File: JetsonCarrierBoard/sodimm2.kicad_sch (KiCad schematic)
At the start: 1 part

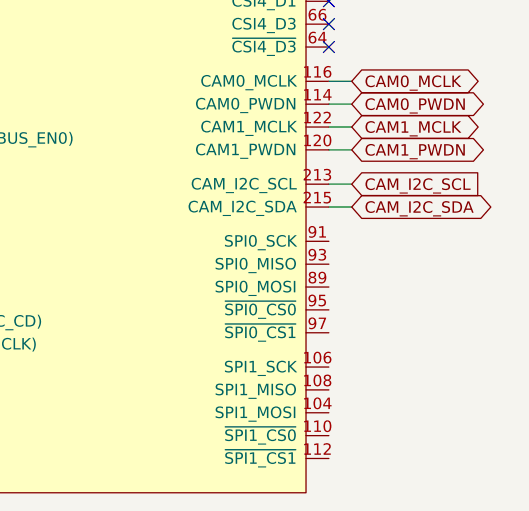
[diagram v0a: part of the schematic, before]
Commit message: IMU wiring
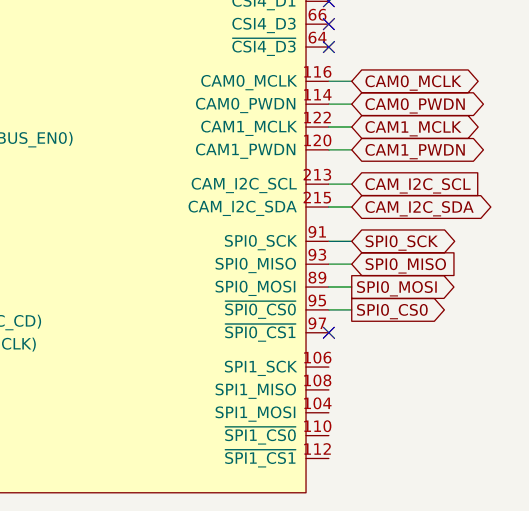
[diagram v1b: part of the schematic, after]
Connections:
- net SPI0_MOSI: now reaches J?.89 (SPI0_MOSI)
- net SPI0_SCK: now reaches J?.91 (SPI0_SCK)
- net SPI0_MISO: now reaches J?.93 (SPI0_MISO)
- net SPI0_CS0: now reaches J?.95 (~{SPI0_CS0})
- no-connect marks 39 -> 40
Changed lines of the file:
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@@
   (no_connect (at 170.18 54.61))
   (no_connect (at 170.18 57.15))
+  (no_connect (at 170.18 148.59))
   (no_connect (at 170.18 90.17))
   (no_connect (at 170.18 93.98))
@@
     (stroke (width 0) (type default) (color 0 0 0 0))
   )
+  (wire (pts (xy 170.18 138.43) (xy 172.72 138.43))
+    (stroke (width 0) (type default) (color 0 0 0 0))
+  )
   (wire (pts (xy 170.18 120.65) (xy 172.72 120.65))
     (stroke (width 0) (type default) (color 0 0 0 0))
@@
     (stroke (width 0) (type default) (color 0 0 0 0))
   )
+  (wire (pts (xy 170.18 146.05) (xy 172.72 146.05))
+    (stroke (width 0) (type default) (color 0 0 0 0))
+  )
   (wire (pts (xy 170.18 134.62) (xy 172.72 134.62))
     (stroke (width 0) (type default) (color 0 0 0 0))
@@
     (stroke (width 0) (type default) (color 0 0 0 0))
   )
+  (wire (pts (xy 170.18 143.51) (xy 172.72 143.51))
+    (stroke (width 0) (type default) (color 0 0 0 0))
+  )
   (wire (pts (xy 170.18 38.1) (xy 172.72 38.1))
     (stroke (width 0) (type default) (color 0 0 0 0))
@@
     (stroke (width 0) (type default) (color 0 0 0 0))
   )
+  (wire (pts (xy 170.18 140.97) (xy 172.72 140.97))
+    (stroke (width 0) (type default) (color 0 0 0 0))
+  )
   (wire (pts (xy 107.95 54.61) (xy 116.84 54.61))
     (stroke (width 0) (type default) (color 0 0 0 0))
@@
     )
   )
+  (global_label "SPI0_SCK" (shape bidirectional) (at 172.72 138.43 0) (fields_autoplaced)
+    (effects (font (size 1.27 1.27)) (justify left))
+    (property "Intersheet References" "${INTERSHEET_REFS}" (id 0) (at 184.1441 138.3506 0)
+      (effects (font (size 1.27 1.27)) (justify left) hide)
+    )
+  )
   (global_label "CAM0_PWDN" (shape bidirectional) (at 172.72 123.19 0) (fields_autoplaced)
     (effects (font (size 1.27 1.27)) (justify left))
@@
     )
   )
+  (global_label "SPI0_CS0" (shape output) (at 172.72 146.05 0) (fields_autoplaced)
+    (effects (font (size 1.27 1.27)) (justify left))
+    (property "Intersheet References" "${INTERSHEET_REFS}" (id 0) (at 184.0836 145.9706 0)
+      (effects (font (size 1.27 1.27)) (justify left) hide)
+    )
+  )
   (global_label "I2S1_SCLK" (shape bidirectional) (at 107.95 66.04 180) (fields_autoplaced)
     (effects (font (size 1.27 1.27)) (justify right))
@@
     )
   )
+  (global_label "SPI0_MISO" (shape input) (at 172.72 140.97 0) (fields_autoplaced)
+    (effects (font (size 1.27 1.27)) (justify left))
+    (property "Intersheet References" "${INTERSHEET_REFS}" (id 0) (at 184.9907 140.8906 0)
+      (effects (font (size 1.27 1.27)) (justify left) hide)
+    )
+  )
   (global_label "MIC_SCK" (shape bidirectional) (at 107.95 54.61 180) (fields_autoplaced)
     (effects (font (size 1.27 1.27)) (justify right))
@@
       (effects (font (size 1.27 1.27)) (justify left) hide)
     )
+  )
+  (global_label "SPI0_MOSI" (shape output) (at 172.72 143.51 0) (fields_autoplaced)
+    (effects (font (size 1.27 1.27)) (justify left))
+    (property "Intersheet References" "${INTERSHEET_REFS}" (id 0) (at 184.9907 143.4306 0)
+      (effects (font (size 1.27 1.27)) (justify left) hide)
+    )

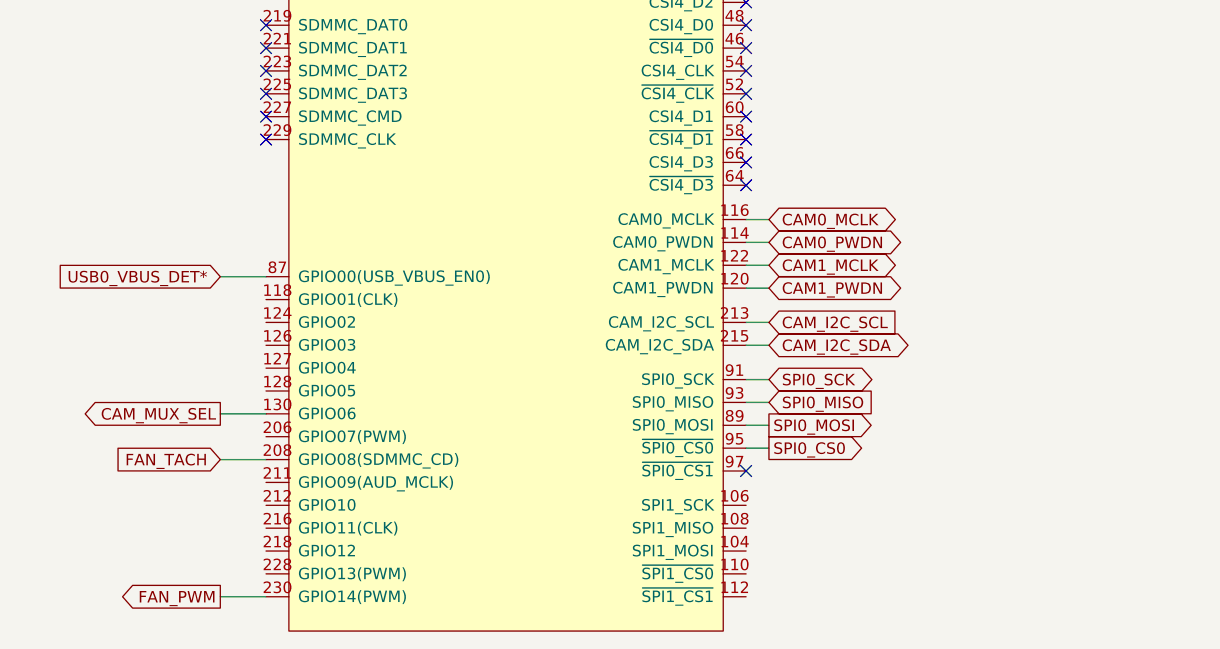
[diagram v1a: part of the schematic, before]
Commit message: Added basic circuits, LED circuit, GPIO pins in GPIO page
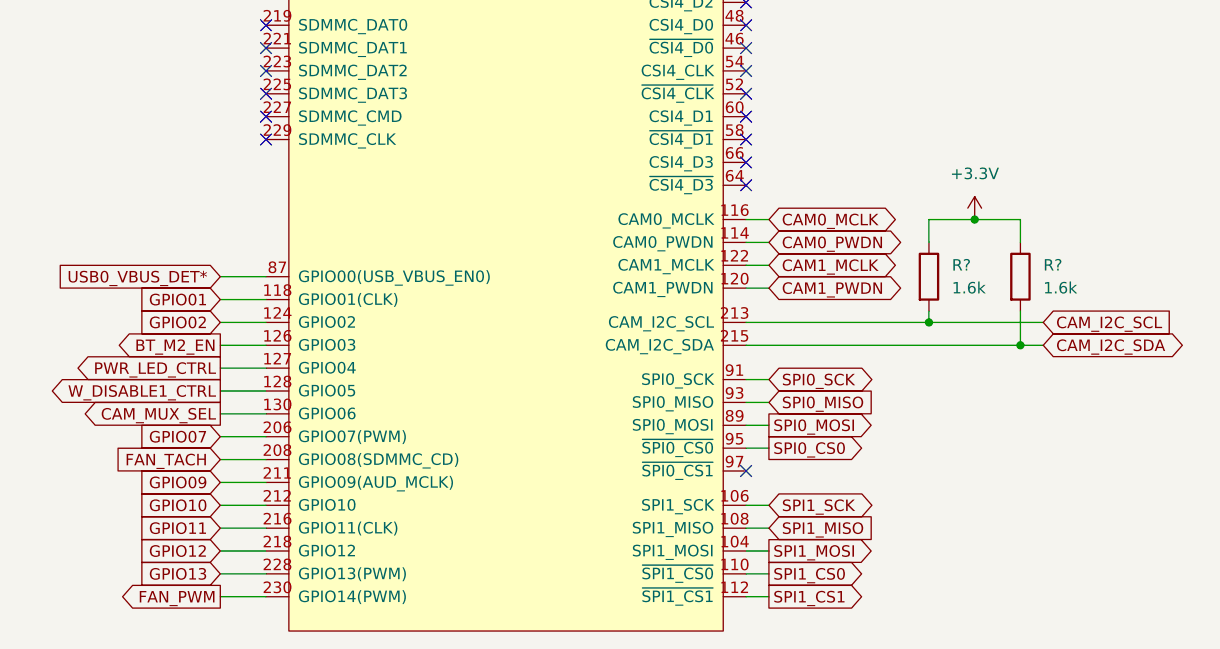
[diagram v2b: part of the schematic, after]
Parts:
- added R? (x2): 1.6k, symbol Device:R
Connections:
- net CAM_I2C_SCL: now also R?.2
- net CAM_I2C_SDA: now also R?.2
- net SPI1_MOSI: now reaches J?.104 (SPI1_MOSI)
- net SPI1_SCK: now reaches J?.106 (SPI1_SCK)
- net SPI1_MISO: now reaches J?.108 (SPI1_MISO)
- net SPI1_CS0: now reaches J?.110 (~{SPI1_CS0})
- net SPI1_CS1: now reaches J?.112 (~{SPI1_CS1})
- net GPIO01: now reaches J?.118 (GPIO01(CLK))
- net GPIO02: now reaches J?.124 (GPIO02)
- net BT_M2_EN: now reaches J?.126 (GPIO03)
- net PWR_LED_CTRL: now reaches J?.127 (GPIO04)
- net W_DISABLE1_CTRL: now reaches J?.128 (GPIO05)
- net GPIO07: now reaches J?.206 (GPIO07(PWM))
- net GPIO09: now reaches J?.211 (GPIO09(AUD_MCLK))
- net GPIO10: now reaches J?.212 (GPIO10)
- net GPIO11: now reaches J?.216 (GPIO11(CLK))
- net GPIO12: now reaches J?.218 (GPIO12)
- net GPIO13: now reaches J?.228 (GPIO13(PWM))
- new net +3.3V: R?.1, R?.1

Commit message: Adding more Title block info and changing main hierarchical page layout
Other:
- title: (none) -> SODIMM Connector 2/3
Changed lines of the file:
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@@
 (kicad_sch (version 20211123) (generator eeschema)
   (paper "A4")
+  (title_block
+    (title "SODIMM Connector 2/3")
+    (date "2022-09-18")
+    (rev "1.0")
+  )
   (junction (at 190.5 132.08) (diameter 0) (color 0 0 0 0)
   )

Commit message: Readability improvements mostly
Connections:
- net SPI1_CS1: no longer names the net of J?.112 (~{SPI1_CS1})
- no-connect marks 40 -> 41
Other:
- note added: "CAM FPC Con"
- note added: "CAM FPC Con Multiplexed"
- note added: "IMU"
- note added: "M.2 BT"
- note added: "Stereo Microphone"
- note added: "USB Type-C Con"
- note added: "uUSB Con"

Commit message: A ton
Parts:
- gave numbers to parts that had none: 3
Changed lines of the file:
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@@
   (symbol (lib_id "power:+3.3V") (at 195.58 120.65 0) (unit 1)
     (in_bom yes) (on_board yes) (fields_autoplaced)
-    (property "Reference" "#PWR?" (id 0) (at 195.58 124.46 0)
+    (property "Reference" "#PWR010" (id 0) (at 195.58 124.46 0)
       (effects (font (size 1.27 1.27)) hide)
     )
@@
   (symbol (lib_id "Device:R") (at 190.5 127 0) (unit 1)
     (in_bom yes) (on_board yes) (fields_autoplaced)
-    (property "Reference" "R?" (id 0) (at 193.04 125.7299 0)
+    (property "Reference" "R5" (id 0) (at 193.04 125.7299 0)
       (effects (font (size 1.27 1.27)) (justify left))
     )
@@
   (symbol (lib_id "Device:R") (at 200.66 127 0) (unit 1)
     (in_bom yes) (on_board yes) (fields_autoplaced)
-    (property "Reference" "R?" (id 0) (at 203.2 125.7299 0)
+    (property "Reference" "R6" (id 0) (at 203.2 125.7299 0)
       (effects (font (size 1.27 1.27)) (justify left))
     )
@@
   (symbol (lib_id "SODIMM_Connector:CON_SODIMM260_JETSON_NANO") (at 143.51 95.25 0) (unit 2)
     (in_bom yes) (on_board yes) (fields_autoplaced)
-    (property "Reference" "J?" (id 0) (at 143.51 19.05 0))
+    (property "Reference" "J1" (id 0) (at 143.51 19.05 0))
     (property "Value" "CON_SODIMM260_JETSON_NANO" (id 1) (at 143.51 21.59 0))
     (property "Footprint" "" (id 2) (at 179.07 52.07 0)
